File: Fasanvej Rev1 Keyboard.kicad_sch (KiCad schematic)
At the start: 138 parts

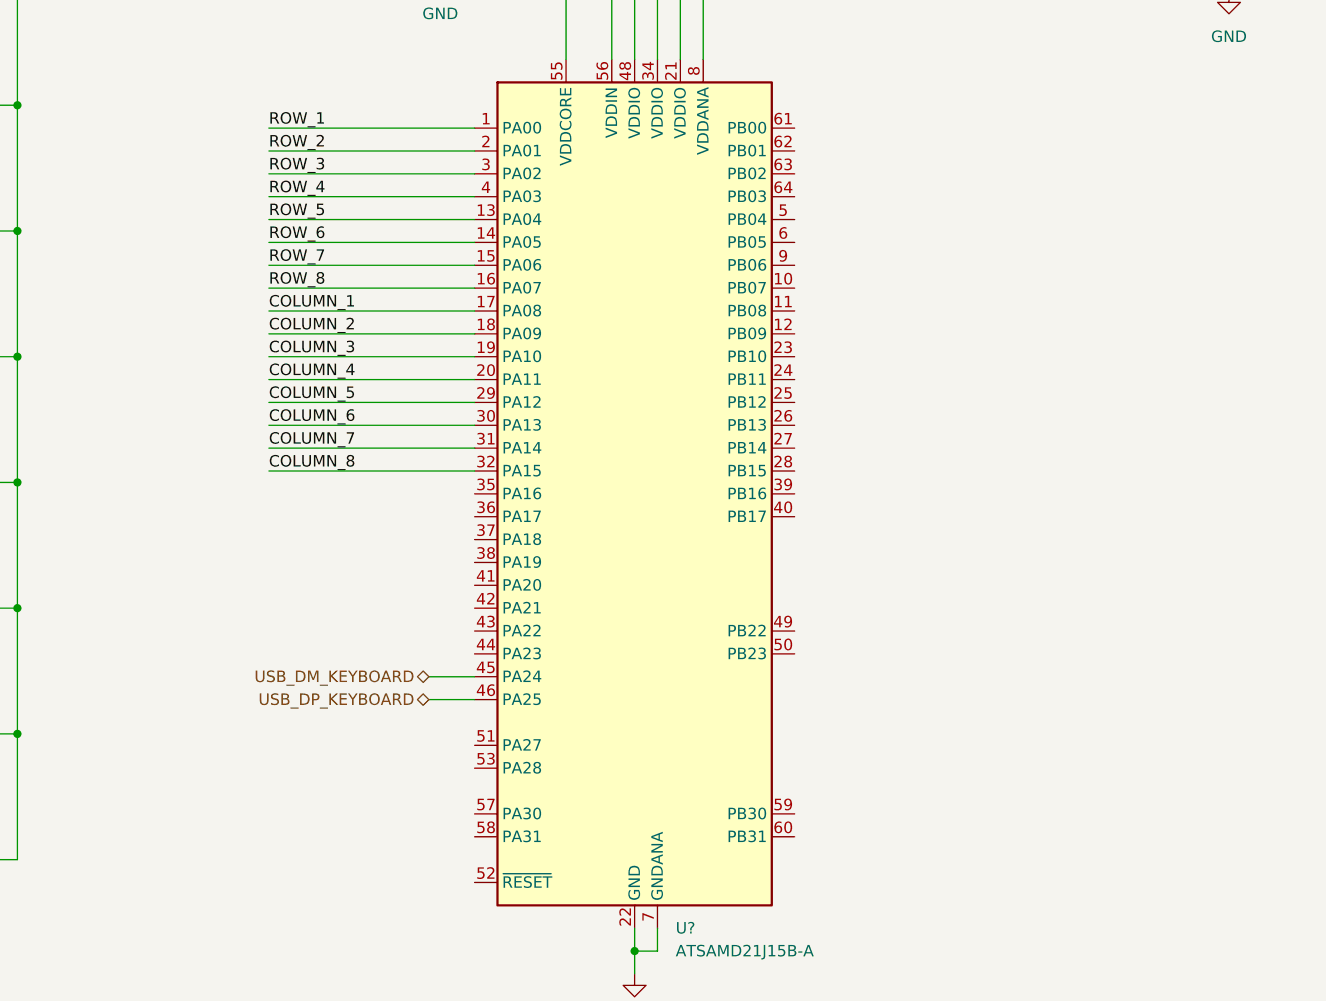
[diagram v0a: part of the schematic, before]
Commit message: Added SPI NOR FLASH. Finished power connections to SoC. Added SWD for keyboard MCU. Improved USB ESD protection. Finished all SoC connections. Added DDR VREF divider.
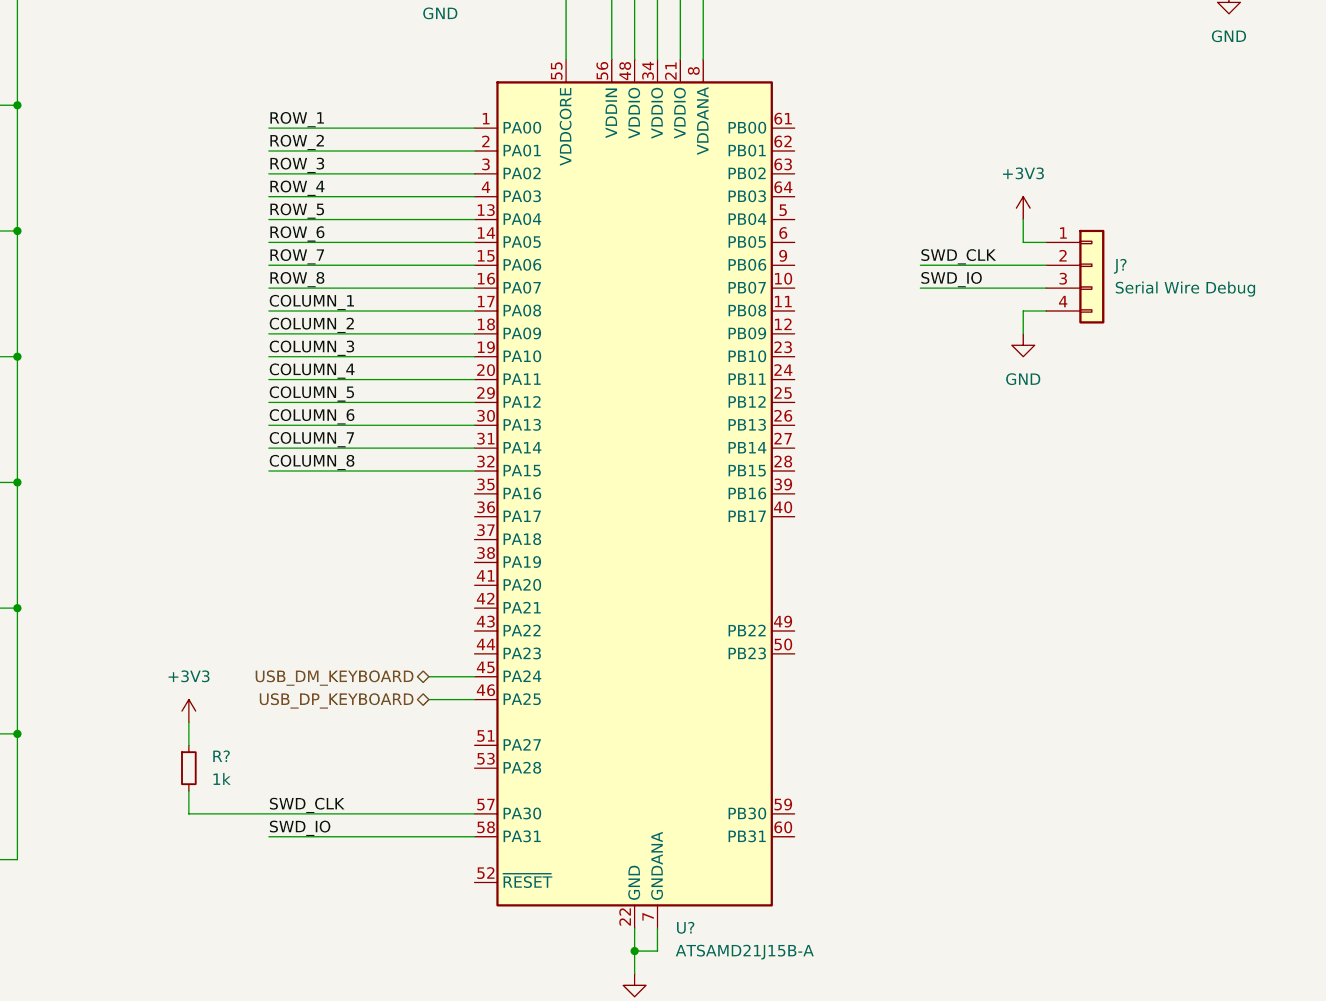
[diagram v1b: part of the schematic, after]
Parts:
- added J?: Serial Wire Debug, Connector_PinHeader_2.54mm:PinHeader_1x04_P2.54mm_Vertical, symbol Connector_Generic:Conn_01x04
- added R?: 1k, Resistor_SMD:R_0603_1608Metric_Pad0.98x0.95mm_HandSolder, symbol Device:R_Small
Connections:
- net +3V3: now also J?.1 (Pin_1), R?.1
- net GND: now also J?.4 (Pin_4)
- net SWD_CLK: now reaches U?.57 (PA30)
- net SWD_CLK: now also J?.2 (Pin_2), R?.2
- net SWD_IO: now reaches U?.58 (PA31)
- net SWD_IO: now also J?.3 (Pin_3)
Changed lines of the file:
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@@
     (stroke (width 0) (type default) (color 0 0 0 0))
   )
+  (wire (pts (xy 370.84 77.47) (xy 373.38 77.47))
+    (stroke (width 0) (type default) (color 0 0 0 0))
+  )
   (wire (pts (xy 215.9 124.46) (xy 218.44 124.46))
     (stroke (width 0) (type default) (color 0 0 0 0))
@@
     (stroke (width 0) (type default) (color 0 0 0 0))
   )
+  (wire (pts (xy 287.02 135.89) (xy 309.88 135.89))
+    (stroke (width 0) (type default) (color 0 0 0 0))
+  )
   (wire (pts (xy 172.72 68.58) (xy 175.26 68.58))
     (stroke (width 0) (type default) (color 0 0 0 0))
@@
     (stroke (width 0) (type default) (color 0 0 0 0))
   )
+  (wire (pts (xy 278.13 123.19) (xy 278.13 125.73))
+    (stroke (width 0) (type default) (color 0 0 0 0))
+  )
   (wire (pts (xy 119.38 138.43) (xy 116.84 138.43))
     (stroke (width 0) (type default) (color 0 0 0 0))
@@
     (stroke (width 0) (type default) (color 0 0 0 0))
   )
+  (wire (pts (xy 370.84 69.85) (xy 373.38 69.85))
+    (stroke (width 0) (type default) (color 0 0 0 0))
+  )
   (wire (pts (xy 238.76 40.64) (xy 236.22 40.64))
     (stroke (width 0) (type default) (color 0 0 0 0))
@@
     (stroke (width 0) (type default) (color 0 0 0 0))
   )
+  (wire (pts (xy 370.84 80.01) (xy 370.84 77.47))
+    (stroke (width 0) (type default) (color 0 0 0 0))
+  )
   (wire (pts (xy 377.19 29.21) (xy 377.19 31.75))
     (stroke (width 0) (type default) (color 0 0 0 0))
@@
     (stroke (width 0) (type default) (color 0 0 0 0))
   )
+  (wire (pts (xy 359.41 74.93) (xy 373.38 74.93))
+    (stroke (width 0) (type default) (color 0 0 0 0))
+  )
   (wire (pts (xy 182.88 40.64) (xy 180.34 40.64))
     (stroke (width 0) (type default) (color 0 0 0 0))
@@
     (stroke (width 0) (type default) (color 0 0 0 0))
   )
+  (wire (pts (xy 278.13 130.81) (xy 278.13 133.35))
+    (stroke (width 0) (type default) (color 0 0 0 0))
+  )
   (wire (pts (xy 208.28 85.09) (xy 236.22 85.09))
     (stroke (width 0) (type default) (color 0 0 0 0))
@@
     (stroke (width 0) (type default) (color 0 0 0 0))
   )
+  (wire (pts (xy 278.13 133.35) (xy 309.88 133.35))
+    (stroke (width 0) (type default) (color 0 0 0 0))
+  )
   (wire (pts (xy 63.5 124.46) (xy 63.5 138.43))
     (stroke (width 0) (type default) (color 0 0 0 0))
@@
     (stroke (width 0) (type default) (color 0 0 0 0))
   )
+  (wire (pts (xy 359.41 72.39) (xy 373.38 72.39))
+    (stroke (width 0) (type default) (color 0 0 0 0))
+  )
   (wire (pts (xy 172.72 82.55) (xy 175.26 82.55))
     (stroke (width 0) (type default) (color 0 0 0 0))
@@
     (stroke (width 0) (type default) (color 0 0 0 0))
   )
+  (wire (pts (xy 370.84 67.31) (xy 370.84 69.85))
+    (stroke (width 0) (type default) (color 0 0 0 0))
+  )
   (wire (pts (xy 127 54.61) (xy 124.46 54.61))
     (stroke (width 0) (type default) (color 0 0 0 0))
@@
     (effects (font (size 1.27 1.27)) (justify left bottom))
   )
+  (label "SWD_CLK" (at 287.02 133.35 0)
+    (effects (font (size 1.27 1.27)) (justify left bottom))
+  )
   (label "COLUMN_5" (at 287.02 87.63 0)
     (effects (font (size 1.27 1.27)) (justify left bottom))
   )
+  (label "SWD_IO" (at 359.41 74.93 0)
+    (effects (font (size 1.27 1.27)) (justify left bottom))
+  )
   (label "COLUMN_1" (at 50.8 26.67 0)
     (effects (font (size 1.27 1.27)) (justify left bottom))
@@
     (effects (font (size 1.27 1.27)) (justify left bottom))
   )
+  (label "SWD_IO" (at 287.02 135.89 0)
+    (effects (font (size 1.27 1.27)) (justify left bottom))
+  )
   (label "ROW_2" (at 287.02 59.69 0)
     (effects (font (size 1.27 1.27)) (justify left bottom))
@@
     (effects (font (size 1.27 1.27)) (justify left bottom))
   )
+  (label "SWD_CLK" (at 359.41 72.39 0)
+    (effects (font (size 1.27 1.27)) (justify left bottom))
+  )
   (label "ROW_6" (at 29.21 113.03 0)
     (effects (font (size 1.27 1.27)) (justify left bottom))
@@
     (pin "2")
   )
+  (symbol (lib_id "power:+3V3") (at 370.84 67.31 0) (unit 1)
+    (in_bom yes) (on_board yes) (fields_autoplaced)
+    (property "Reference" "#PWR?" (id 0) (at 370.84 71.12 0)
+      (effects (font (size 1.27 1.27)) hide)
+    )
+    (property "Value" "+3V3" (id 1) (at 370.84 62.23 0))
+    (property "Footprint" "" (id 2) (at 370.84 67.31 0)
+      (effects (font (size 1.27 1.27)) hide)
+    )
+    (property "Datasheet" "" (id 3) (at 370.84 67.31 0)
+      (effects (font (size 1.27 1.27)) hide)
+    )
+    (pin "1")
+  )
   (symbol (lib_id "Device:D_Small") (at 101.6 124.46 0) (unit 1)
     (in_bom yes) (on_board yes) (fields_autoplaced)
@@
     (pin "2")
   )
+  (symbol (lib_id "Device:R_Small") (at 278.13 128.27 0) (unit 1)
+    (in_bom yes) (on_board yes) (fields_autoplaced)
+    (property "Reference" "R?" (id 0) (at 280.67 126.9999 0)
+      (effects (font (size 1.27 1.27)) (justify left))
+    )
+    (property "Value" "1k" (id 1) (at 280.67 129.5399 0)
+      (effects (font (size 1.27 1.27)) (justify left))
+    )
+    (property "Footprint" "Resistor_SMD:R_0603_1608Metric_Pad0.98x0.95mm_HandSolder" (id 2) (at 278.13 128.27 0)
+      (effects (font (size 1.27 1.27)) hide)
+    )
+    (property "Datasheet" "~" (id 3) (at 278.13 128.27 0)
+      (effects (font (size 1.27 1.27)) hide)
+    )
+    (pin "1")
+    (pin "2")
+  )
   (symbol (lib_id "Switch:SW_Push") (at 223.52 138.43 0) (unit 1)
     (in_bom yes) (on_board yes) (fields_autoplaced)
@@
     (pin "2")
   )
+  (symbol (lib_id "Connector_Generic:Conn_01x04") (at 378.46 72.39 0) (unit 1)
+    (in_bom yes) (on_board yes) (fields_autoplaced)
+    (property "Reference" "J?" (id 0) (at 381 72.3899 0)
+      (effects (font (size 1.27 1.27)) (justify left))
+    )
+    (property "Value" "Serial Wire Debug" (id 1) (at 381 74.9299 0)
+      (effects (font (size 1.27 1.27)) (justify left))
+    )
+    (property "Footprint" "Connector_PinHeader_2.54mm:PinHeader_1x04_P2.54mm_Vertical" (id 2) (at 378.46 72.39 0)
+      (effects (font (size 1.27 1.27)) hide)
+    )
+    (property "Datasheet" "~" (id 3) (at 378.46 72.39 0)
+      (effects (font (size 1.27 1.27)) hide)
+    )
+    (pin "1")
+    (pin "2")
+    (pin "3")
+    (pin "4")
+  )
   (symbol (lib_id "Device:C_Small") (at 341.63 34.29 0) (unit 1)
     (in_bom yes) (on_board yes) (fields_autoplaced)
@@
     (pin "2")
   )
+  (symbol (lib_id "power:+3V3") (at 278.13 123.19 0) (unit 1)
+    (in_bom yes) (on_board yes) (fields_autoplaced)
+    (property "Reference" "#PWR?" (id 0) (at 278.13 127 0)
+      (effects (font (size 1.27 1.27)) hide)
+    )
+    (property "Value" "+3V3" (id 1) (at 278.13 118.11 0))
+    (property "Footprint" "" (id 2) (at 278.13 123.19 0)
+      (effects (font (size 1.27 1.27)) hide)
+    )
+    (property "Datasheet" "" (id 3) (at 278.13 123.19 0)
+      (effects (font (size 1.27 1.27)) hide)
+    )
+    (pin "1")
+  )
   (symbol (lib_id "Device:C_Small") (at 359.41 34.29 0) (unit 1)
     (in_bom yes) (on_board yes) (fields_autoplaced)
@@
     (pin "2")
   )
+  (symbol (lib_id "power:GND") (at 370.84 80.01 0) (unit 1)
+    (in_bom yes) (on_board yes) (fields_autoplaced)
+    (property "Reference" "#PWR?" (id 0) (at 370.84 86.36 0)
+      (effects (font (size 1.27 1.27)) hide)
+    )
+    (property "Value" "GND" (id 1) (at 370.84 85.09 0))
+    (property "Footprint" "" (id 2) (at 370.84 80.01 0)
+      (effects (font (size 1.27 1.27)) hide)
+    )
+    (property "Datasheet" "" (id 3) (at 370.84 80.01 0)
+      (effects (font (size 1.27 1.27)) hide)
+    )
+    (pin "1")
+  )
   (symbol (lib_id "Switch:SW_Push") (at 55.88 68.58 0) (unit 1)

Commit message: Finished schematics. Pending validation.
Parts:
- added R?: 10k, Resistor_SMD:R_0603_1608Metric_Pad0.98x0.95mm_HandSolder, symbol Device:R_Small
- SW?: footprint (none) -> Button_Switch_SMD:SW_SPST_TL3342
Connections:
- net +3V3: now also R?.1
- net at U?.52 (~{RESET}): now also R?.2
- no-connect marks 0 -> 32
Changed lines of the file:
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@@
   (junction (at 152.4 113.03) (diameter 0) (color 0 0 0 0)
   )
+  (no_connect (at 309.88 113.03))
+  (no_connect (at 309.88 115.57))
+  (no_connect (at 309.88 125.73))
+  (no_connect (at 309.88 128.27))
+  (no_connect (at 309.88 97.79))
+  (no_connect (at 309.88 100.33))
+  (no_connect (at 309.88 102.87))
+  (no_connect (at 309.88 105.41))
+  (no_connect (at 309.88 107.95))
+  (no_connect (at 309.88 110.49))
+  (no_connect (at 345.44 135.89))
+  (no_connect (at 345.44 133.35))
+  (no_connect (at 345.44 115.57))
+  (no_connect (at 345.44 113.03))
+  (no_connect (at 345.44 97.79))
+  (no_connect (at 345.44 100.33))
+  (no_connect (at 345.44 57.15))
+  (no_connect (at 345.44 59.69))
+  (no_connect (at 345.44 62.23))
+  (no_connect (at 345.44 64.77))
+  (no_connect (at 345.44 67.31))
+  (no_connect (at 345.44 69.85))
+  (no_connect (at 345.44 72.39))
+  (no_connect (at 345.44 74.93))
+  (no_connect (at 345.44 77.47))
+  (no_connect (at 345.44 80.01))
+  (no_connect (at 345.44 82.55))
+  (no_connect (at 345.44 85.09))
+  (no_connect (at 345.44 87.63))
+  (no_connect (at 345.44 90.17))
+  (no_connect (at 345.44 92.71))
+  (no_connect (at 345.44 95.25))
   (wire (pts (xy 124.46 124.46) (xy 124.46 127))
     (stroke (width 0) (type default) (color 0 0 0 0))
@@
     (stroke (width 0) (type default) (color 0 0 0 0))
   )
+  (wire (pts (xy 270.51 123.19) (xy 270.51 125.73))
+    (stroke (width 0) (type default) (color 0 0 0 0))
+  )
   (wire (pts (xy 152.4 138.43) (xy 152.4 140.97))
     (stroke (width 0) (type default) (color 0 0 0 0))
@@
     (stroke (width 0) (type default) (color 0 0 0 0))
   )
+  (wire (pts (xy 270.51 130.81) (xy 270.51 140.97))
+    (stroke (width 0) (type default) (color 0 0 0 0))
+  )
   (wire (pts (xy 393.7 29.21) (xy 386.08 29.21))
     (stroke (width 0) (type default) (color 0 0 0 0))
@@
     (stroke (width 0) (type default) (color 0 0 0 0))
   )
+  (wire (pts (xy 270.51 140.97) (xy 309.88 140.97))
+    (stroke (width 0) (type default) (color 0 0 0 0))
+  )
   (wire (pts (xy 29.21 140.97) (xy 40.64 140.97))
     (stroke (width 0) (type default) (color 0 0 0 0))
@@
     (pin "2")
   )
+  (symbol (lib_id "Device:R_Small") (at 270.51 128.27 0) (unit 1)
+    (in_bom yes) (on_board yes) (fields_autoplaced)
+    (property "Reference" "R?" (id 0) (at 273.05 126.9999 0)
+      (effects (font (size 1.27 1.27)) (justify left))
+    )
+    (property "Value" "10k" (id 1) (at 273.05 129.5399 0)
+      (effects (font (size 1.27 1.27)) (justify left))
+    )
+    (property "Footprint" "Resistor_SMD:R_0603_1608Metric_Pad0.98x0.95mm_HandSolder" (id 2) (at 270.51 128.27 0)
+      (effects (font (size 1.27 1.27)) hide)
+    )
+    (property "Datasheet" "~" (id 3) (at 270.51 128.27 0)
+      (effects (font (size 1.27 1.27)) hide)
+    )
+    (pin "1")
+    (pin "2")
+  )
   (symbol (lib_id "Switch:SW_Push") (at 55.88 82.55 0) (unit 1)
     (in_bom yes) (on_board yes) (fields_autoplaced)
@@
     (property "Reference" "SW?" (id 0) (at 251.46 33.02 0))
     (property "Value" "SW_Push" (id 1) (at 251.46 42.164 0))
-    (property "Footprint" "" (id 2) (at 251.46 35.56 0)
+    (property "Footprint" "Button_Switch_SMD:SW_SPST_TL3342" (id 2) (at 251.46 35.56 0)
       (effects (font (size 1.27 1.27)) hide)
     )
@@
     (pin "2")
   )
+  (symbol (lib_id "power:+3V3") (at 270.51 123.19 0) (unit 1)
+    (in_bom yes) (on_board yes) (fields_autoplaced)
+    (property "Reference" "#PWR?" (id 0) (at 270.51 127 0)
+      (effects (font (size 1.27 1.27)) hide)
+    )
+    (property "Value" "+3V3" (id 1) (at 270.51 118.11 0))
+    (property "Footprint" "" (id 2) (at 270.51 123.19 0)
+      (effects (font (size 1.27 1.27)) hide)
+    )
+    (property "Datasheet" "" (id 3) (at 270.51 123.19 0)
+      (effects (font (size 1.27 1.27)) hide)
+    )
+    (pin "1")
+  )
   (symbol (lib_id "Device:D_Small") (at 129.54 54.61 0) (unit 1)
